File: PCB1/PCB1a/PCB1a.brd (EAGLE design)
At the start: 125.6 x 84.2 mm, 10 parts, among them J1 691357310006B, J2 618009231421, J3 ESP32_DEVC_MIN_LEFT, J4 ESP32_DEVC_MIN_RIGHT, U8 74AHCT245, U9 74AHCT245

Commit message: intermediate. commit.
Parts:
- added C1: 470uF, Wurth_Capacitors_WCAP-AS5H:WCAP-AS5H_10X10.5(DXL)
- added C15: 47nF, Wurth_Capacitors_WCAP-CSGP:WCAP-CSGP_0805_H0.8_R
- added C17, C19: 100nF, Wurth_Capacitors_WCAP-CSGP:WCAP-CSGP_0805_H0.8_R
- added C3, C4, C6, C7, C8: 100nF, Discrete:C0603
- added D1: 5V, Wurth_EMC Components_WE-TVSP:WE-TVSP_DO-214AB_BIDIRECTIONAL
- added D11: 24Vdc, Wurth_EMC Components_WE-TVS:WE-TVS_SOT23-3L
- added R1, R3: 60R, resistor:R0805
- added U2: MAX232D, IC:SOIC16
- added U4: TLE9250VSJ, TLE9250VSJ:SOIC127P602X173-8N-V
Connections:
- removed net CAN_H: J1.6
- removed net CAN_L: J1.5
- removed net N$12: J3.23A, J3.23B
- removed net N$18: J4.35A, J4.35B
- removed net N$19: J4.32A, J4.32B
- removed net N$4: J3.5A, J3.5B
- new net +3V3: C19.1, U4.5
- new net 232_RX: J2.2, U2.13
- new net 232_TX: J2.3, U2.14
- new net CAN1_RXD: J4.35A, J4.35B, U4.4
- new net CAN1_TXD: J3.5A, J3.5B, U4.1
- new net CAN_N: D11.1, J1.5, R3.2, U4.6
- new net CAN_P: D11.2, J1.6, R1.2, U4.7
- new net N$20: C15.1, R1.1, R3.1
- new net N$33: C6.2, U2.1
- new net N$34: C6.1, U2.3
- new net N$35: C7.2, U2.4
- new net N$36: C7.1, U2.5
- new net N$37: C4.1, U2.2
- new net N$38: C8.1, U2.6
- new net N$39: U2.9
- new net N$40: U2.10
- new net N$46: U2.7
- new net N$47: U2.8
- new net VCC: C3.1, C4.2, U2.16
- net +5V: now also C1.1, C17.1, D1.2, U4.3
- net GND: now also C1.2, C15.2, C17.2, C19.2, C3.2, C8.2, D1.1, D11.3, U2.15, U4.2, U4.8
- net RX: now also J4.32A, J4.32B, U2.12; no longer J2.2
- net TX: now also J3.23A, J3.23B, U2.11; no longer J2.3
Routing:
- net RX: track 0.00 -> 59.8 mm, vias 0 -> 1
- net CAN1_RXD: track 0.00 -> 49.8 mm
- net TX: track 0.00 -> 28.4 mm, vias 0 -> 1
- net 232_TX: track 0.00 -> 18.8 mm
- net 232_RX: track 0.00 -> 18.2 mm
- net CAN1_TXD: track 0.00 -> 12.2 mm
- net VCC: track 0.00 -> 6.43 mm
- net GND: track 48.7 -> 54.2 mm, vias 14 -> 16
- net N$37: track 0.00 -> 5.50 mm
- net N$38: track 0.00 -> 3.13 mm
- net N$34: track 0.00 -> 3.13 mm
- net N$33: track 0.00 -> 3.13 mm
- net N$36: track 0.00 -> 2.97 mm
- net N$35: track 0.00 -> 2.97 mm
- net N$4: track 2.54 -> 0.00 mm
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
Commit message: ..
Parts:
- moved C17 0.38 mm to (13.0, -14.3)
- moved C19 0.38 mm to (19.4, -18.2)
- moved R1 0.38 mm to (35.6, -15.2)
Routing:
- net CAN_N: track 0.00 -> 34.5 mm
- net CAN_P: track 0.00 -> 33.8 mm
- net +5V: track 10.5 -> 18.7 mm, vias 4 -> 7
- net N$20: track 0.00 -> 6.05 mm
- net GND: track 54.2 -> 58.5 mm, vias 16 -> 106
- net +3V3: track 0.00 -> 2.06 mm

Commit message: thermals="no"/>
 thermals="no"/>
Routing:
- net GND: vias 106 -> 107
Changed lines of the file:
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@@
 <drawing>
 <settings>
-<setting alwaysvectorfont="yes"/>
+<setting alwaysvectorfont="no"/>
 <setting verticaltext="up"/>
 </settings>
@@
 <via x="-17.399" y="-13.716" extent="1-16" drill="0.35"/>
 <via x="-17.018" y="-16.256" extent="1-16" drill="0.35"/>
+<via x="-10.16" y="-5.08" extent="1-16" drill="0.35"/>
 </signal>
 <signal name="+5V" class="3">

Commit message: ..
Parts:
- C3, C4, C6, C7, C8: device Discrete:C0603 -> Wurth_Capacitors_WCAP-CSGP:WCAP-CSGP_0805_H0.8_R
- moved C6 0.32 mm to (21.0, 11.0)
- moved C8 0.25 mm to (27.9, 11.1)
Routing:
- net GND: track 58.5 -> 58.6 mm, vias 107 -> 255

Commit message: ..
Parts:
- added JP1: JUMPER-SMT_2_NO_SILK_ROUND, SparkFun-Jumpers:SMT-JUMPER_2_NO_SILK_ROUND
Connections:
- new net M1_E_NC: JP1.1, U8.12
- net M1_E: now also JP1.2; no longer U8.12
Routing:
- net M1_E_NC: track 0.00 -> 15.4 mm
- net M1_E: track 47.7 -> 37.3 mm
- net GND: track 58.6 -> 55.2 mm, vias 255 -> 478
- net VCC: track 6.32 -> 4.69 mm

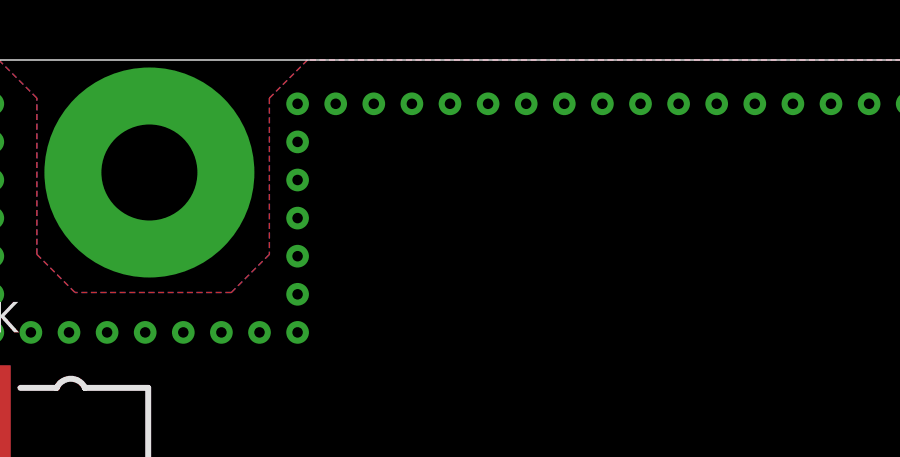
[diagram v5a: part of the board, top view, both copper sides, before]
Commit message: thermals="no"
thermals="no"
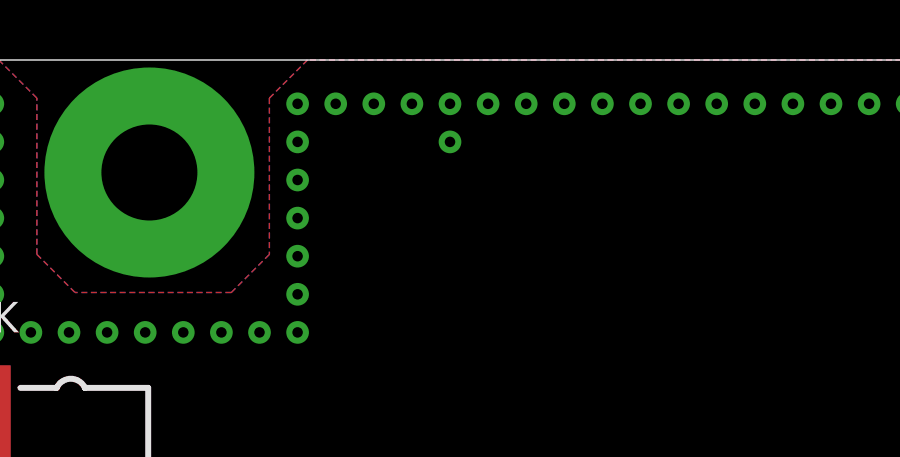
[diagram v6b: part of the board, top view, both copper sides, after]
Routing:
- net GND: vias 478 -> 479

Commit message: .
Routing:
- net GND: vias 479 -> 478
